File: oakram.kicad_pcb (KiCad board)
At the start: 2 copper layers, 43.2 x 54 mm, 11 parts, among them U1 IS41C16105C, U2 IS41C16105C, X1 ZIP40, X2 ZIP40

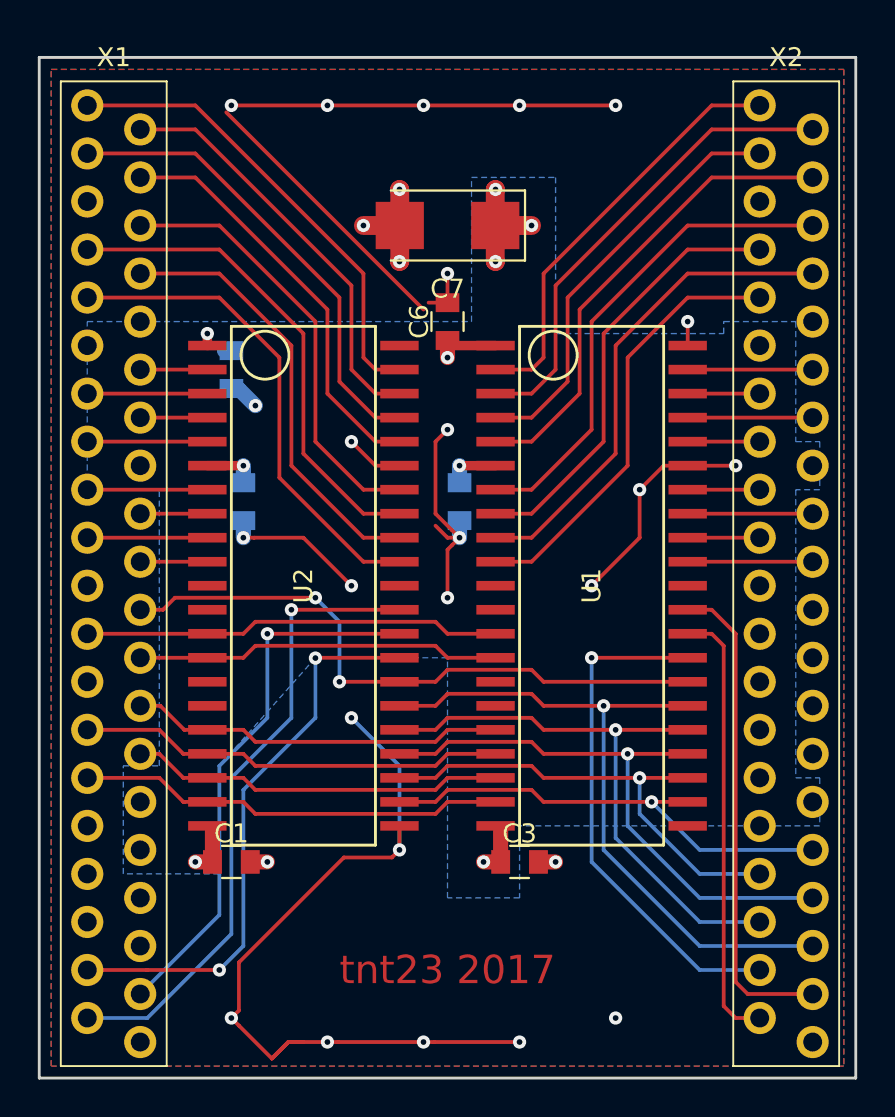
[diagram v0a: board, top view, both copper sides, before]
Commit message: Connector and chip moved
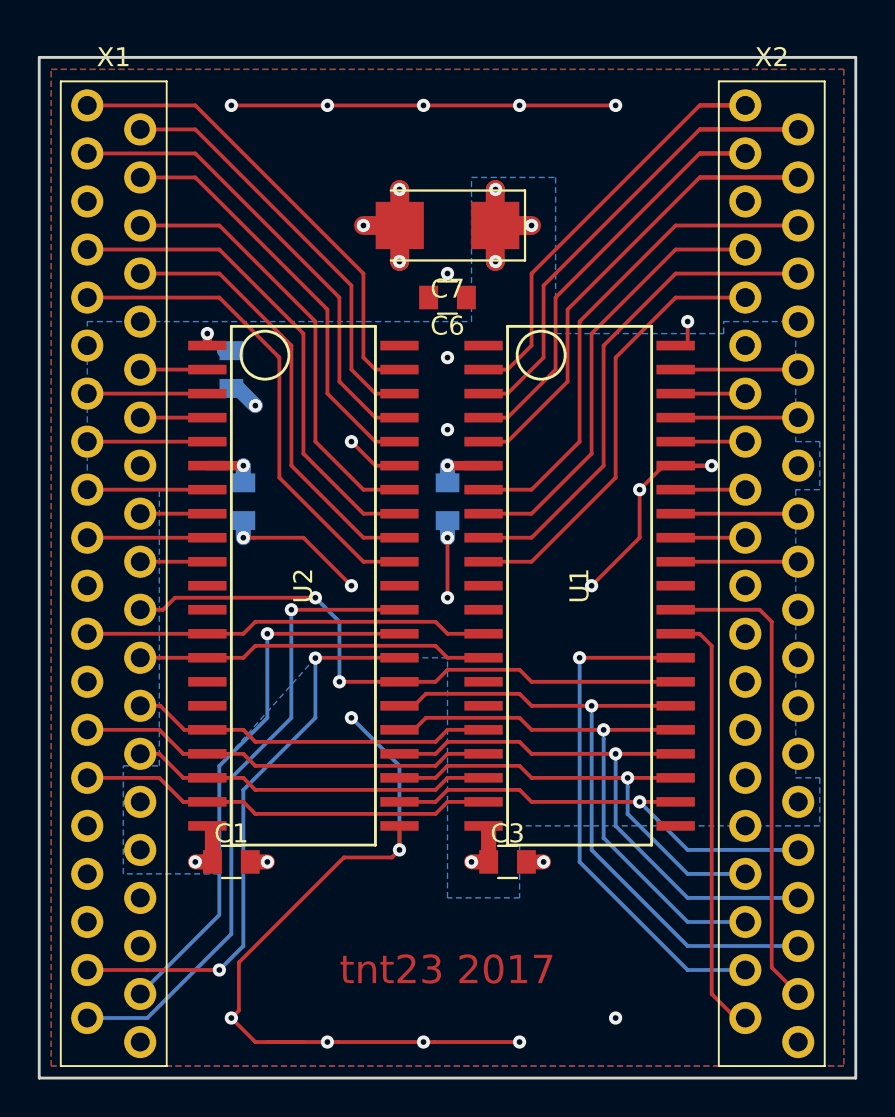
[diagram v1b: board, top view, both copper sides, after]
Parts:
- moved C6 1.27 mm to (141.0, 86.4), turned to 180 degrees
- moved X2 0.76 mm to (158.1, 100.3)
- moved C3 0.63 mm to (144.1, 116.2)
- moved C4 0.63 mm to (141.0, 97.2)
- moved U1 0.63 mm to (148.0, 101.6)
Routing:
- net VSS: track 125.6 -> 98.1 mm
- net /D25: track 24.9 -> 29.7 mm
- net VCC: track 21.8 -> 18.2 mm
- net /D27: track 25.5 -> 29.1 mm
- net /D26: track 22.4 -> 24.4 mm
- net /D24: track 22.4 -> 24.4 mm
- net /~CAS3: track 25.8 -> 25.0 mm
- net /D30: track 26.3 -> 25.5 mm
- net /A5: track 25.3 -> 26.0 mm
- net /A4: track 25.7 -> 25.1 mm
- net /~OE: track 57.2 -> 57.7 mm
- net /D21: track 6.99 -> 6.48 mm
- net /D16: track 6.99 -> 6.48 mm
- net /A8: track 36.9 -> 36.4 mm

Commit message: Board resized
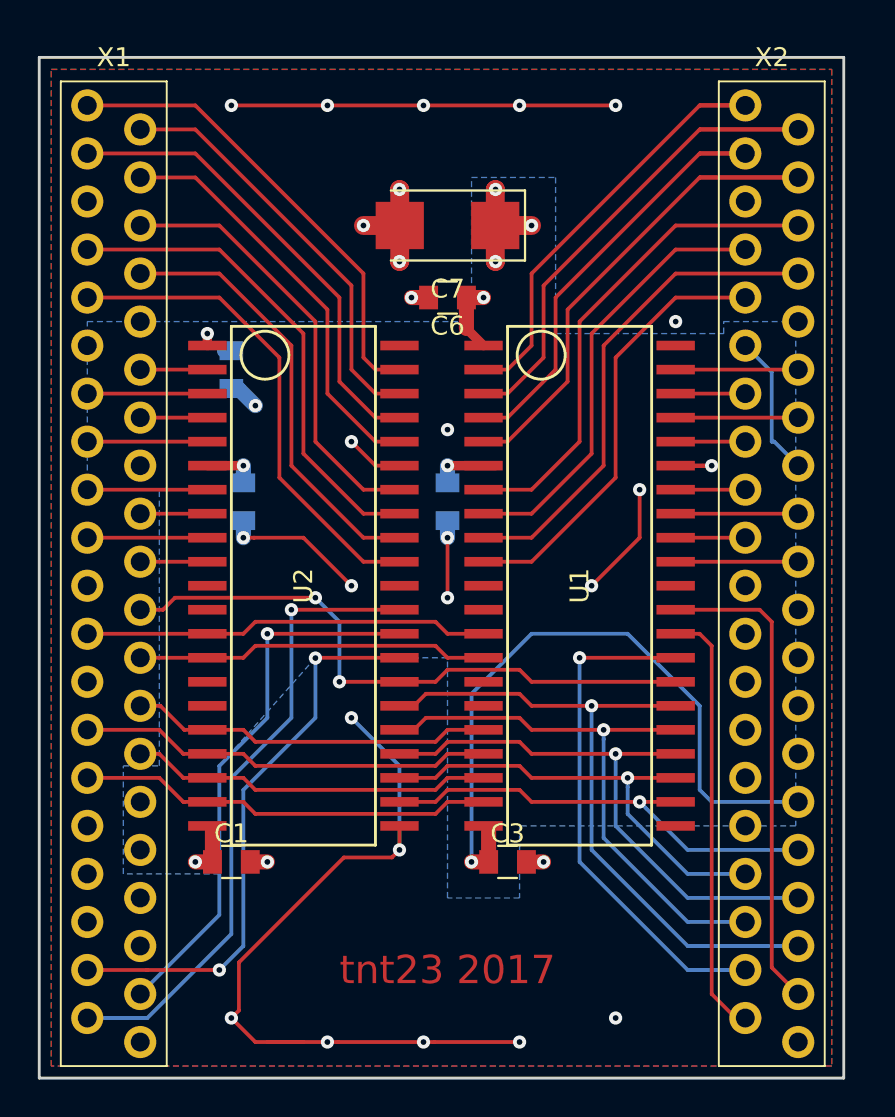
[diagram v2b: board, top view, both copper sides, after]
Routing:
- net VCC: track 18.2 -> 63.7 mm
- net VSS: track 98.1 -> 95.9 mm
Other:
- board size 43.2 x 54 mm -> 42.5 x 54 mm
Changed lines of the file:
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@@
   (thickness 1.6)
   (drawings 8)
-  (tracks 347)
+  (tracks 361)
   (zones 0)
   (modules 11)
@@
   (36 B.SilkS user)
   (37 F.SilkS user)
-  (38 B.Mask user)
-  (39 F.Mask user)
+  (38 B.Mask user hide)
+  (39 F.Mask user hide)
   (40 Dwgs.User user)
   (41 Cmts.User user)
@@
 )
 (setup
-  (last_trace_width 0.2)
+  (last_trace_width 0.8)
   (user_trace_width 0.2)
   (user_trace_width 0.3)
@@
     (effects (font (size 1.5 1.5) (thickness 0.3)))
   )
-  (dimension 43.18 (width 0.3) (layer Cmts.User)
-    (gr_text "43.180 mm" (at 140.97 134.699999) (layer Cmts.User)
+  (dimension 42.545 (width 0.3) (layer Cmts.User)
+    (gr_text "42.545 mm" (at 140.6525 134.7) (layer Cmts.User)
       (effects (font (size 1.5 1.5) (thickness 0.3)))
     )
-    (feature1 (pts (xy 162.56 127.635) (xy 162.56 136.049999)))
-    (feature2 (pts (xy 119.38 127.635) (xy 119.38 136.049999)))
-    (crossbar (pts (xy 119.38 133.349999) (xy 162.56 133.349999)))
-    (arrow1a (pts (xy 162.56 133.349999) (xy 161.433496 133.93642)))
-    (arrow1b (pts (xy 162.56 133.349999) (xy 161.433496 132.763578)))
-    (arrow2a (pts (xy 119.38 133.349999) (xy 120.506504 133.93642)))
-    (arrow2b (pts (xy 119.38 133.349999) (xy 120.506504 132.763578)))
+    (feature1 (pts (xy 161.925 127.635) (xy 161.925 136.05)))
+    (feature2 (pts (xy 119.38 127.635) (xy 119.38 136.05)))
+    (crossbar (pts (xy 119.38 133.35) (xy 161.925 133.35)))
+    (arrow1a (pts (xy 161.925 133.35) (xy 160.798496 133.936421)))
+    (arrow1b (pts (xy 161.925 133.35) (xy 160.798496 132.763579)))
+    (arrow2a (pts (xy 119.38 133.35) (xy 120.506504 133.936421)))
+    (arrow2b (pts (xy 119.38 133.35) (xy 120.506504 132.763579)))
   )
   (dimension 53.975 (width 0.3) (layer Cmts.User)
-    (gr_text "53.975 mm" (at 172.8 100.6475 270) (layer Cmts.User)
+    (gr_text "53.975 mm" (at 172.165 100.6475 270) (layer Cmts.User)
       (effects (font (size 1.5 1.5) (thickness 0.3)))
     )
-    (feature1 (pts (xy 162.56 127.635) (xy 174.15 127.635)))
-    (feature2 (pts (xy 162.56 73.66) (xy 174.15 73.66)))
-    (crossbar (pts (xy 171.45 73.66) (xy 171.45 127.635)))
-    (arrow1a (pts (xy 171.45 127.635) (xy 170.863579 126.508496)))
-    (arrow1b (pts (xy 171.45 127.635) (xy 172.036421 126.508496)))
-    (arrow2a (pts (xy 171.45 73.66) (xy 170.863579 74.786504)))
-    (arrow2b (pts (xy 171.45 73.66) (xy 172.036421 74.786504)))
+    (feature1 (pts (xy 161.925 127.635) (xy 173.515 127.635)))
+    (feature2 (pts (xy 161.925 73.66) (xy 173.515 73.66)))
+    (crossbar (pts (xy 170.815 73.66) (xy 170.815 127.635)))
+    (arrow1a (pts (xy 170.815 127.635) (xy 170.228579 126.508496)))
+    (arrow1b (pts (xy 170.815 127.635) (xy 171.401421 126.508496)))
+    (arrow2a (pts (xy 170.815 73.66) (xy 170.228579 74.786504)))
+    (arrow2b (pts (xy 170.815 73.66) (xy 171.401421 74.786504)))
   )
   (gr_line (start 119.38 127.635) (end 119.38 73.66) (layer Edge.Cuts) (width 0.15))
-  (gr_line (start 162.56 127.635) (end 119.38 127.635) (layer Edge.Cuts) (width 0.15))
-  (gr_line (start 162.56 73.66) (end 162.56 127.635) (layer Edge.Cuts) (width 0.15))
-  (gr_line (start 119.38 73.66) (end 162.56 73.66) (layer Edge.Cuts) (width 0.15))
+  (gr_line (start 161.925 127.635) (end 119.38 127.635) (layer Edge.Cuts) (width 0.15))
+  (gr_line (start 161.925 73.66) (end 161.925 127.635) (layer Edge.Cuts) (width 0.15))
+  (gr_line (start 119.38 73.66) (end 161.925 73.66) (layer Edge.Cuts) (width 0.15))
   (segment (start 138.43 90.17) (end 137.16 90.17) (width 0.2) (layer F.Cu) (net 1))
   (segment (start 137.16 90.17) (end 136.525 89.535) (width 0.2) (layer F.Cu) (net 1))
@@
   (segment (start 145.415 85.09) (end 154.305 76.2) (width 0.2) (layer F.Cu) (net 55))
   (segment (start 154.305 76.2) (end 157.48 76.2) (width 0.2) (layer F.Cu) (net 55))
+  (segment (start 139.97 86.36) (end 139.065 86.36) (width 0.8) (layer F.Cu) (net 56))
+  (via (at 153.035 87.63) (size 0.7) (drill 0.3) (layers F.Cu B.Cu) (net 56))
   (segment (start 154.445026 95.25) (end 154.94 95.25) (width 0.2) (layer F.Cu) (net 56))
   (segment (start 152.4 95.25) (end 154.445026 95.25) (width 0.2) (layer F.Cu) (net 56))
-  (segment (start 151.13 96.52) (end 152.4 95.25) (width 0.2) (layer F.Cu) (net 56))
   (segment (start 153.67 95.25) (end 154.94 95.25) (width 0.2) (layer F.Cu) (net 56))
   (via (at 154.94 95.25) (size 0.7) (drill 0.3) (layers F.Cu B.Cu) (net 56))
@@
   (segment (start 129.939999 124.059999) (end 129.54 124.459998) (width 0.2) (layer F.Cu) (net 56))
   (via (at 140.97 93.345) (size 0.7) (drill 0.3) (layers F.Cu B.Cu) (net 56))
-  (via (at 153.67 87.63) (size 0.7) (drill 0.3) (layers F.Cu B.Cu) (net 56))
-  (segment (start 153.67 88.9) (end 153.67 87.63) (width 0.2) (layer F.Cu) (net 56))
   (via (at 149.86 124.46) (size 0.7) (drill 0.3) (layers F.Cu B.Cu) (net 56))
   (segment (start 130.740685 99.06) (end 130.175 99.06) (width 0.2) (layer F.Cu) (net 56))
@@
   (via (at 129.54 76.2) (size 0.7) (drill 0.3) (layers F.Cu B.Cu) (net 56))
   (via (at 140.97 102.235) (size 0.7) (drill 0.3) (layers F.Cu B.Cu) (net 56))
-  (via (at 140.97 85.09) (size 0.7) (drill 0.3) (layers F.Cu B.Cu) (net 56))
+  (via (at 139.065 86.36) (size 0.7) (drill 0.3) (layers F.Cu B.Cu) (net 56))
   (segment (start 138.43 114.3) (end 138.43 115.57) (width 0.2) (layer F.Cu) (net 56))
   (via (at 138.43 115.57) (size 0.7) (drill 0.3) (layers F.Cu B.Cu) (net 56))
@@
   (segment (start 130.54 116.205) (end 131.445 116.205) (width 0.8) (layer F.Cu) (net 56))
   (via (at 131.445 116.205) (size 0.7) (drill 0.3) (layers F.Cu B.Cu) (net 56))
+  (segment (start 142.875 86.36) (end 141.97 86.36) (width 0.8) (layer F.Cu) (net 57))
+  (via (at 142.875 86.36) (size 0.7) (drill 0.3) (layers F.Cu B.Cu) (net 57))
+  (segment (start 141.97 86.36) (end 141.97 87.995) (width 0.8) (layer F.Cu) (net 57))
+  (segment (start 141.97 87.995) (end 142.875 88.9) (width 0.5) (layer F.Cu) (net 57))
+  (segment (start 142.24 116.205) (end 142.24 107.315) (width 0.2) (layer B.Cu) (net 57))
+  (segment (start 145.415 104.14) (end 150.495 104.14) (width 0.2) (layer B.Cu) (net 57))
+  (segment (start 154.305 112.395) (end 154.94 113.03) (width 0.2) (layer B.Cu) (net 57))
+  (segment (start 142.24 107.315) (end 145.415 104.14) (width 0.2) (layer B.Cu) (net 57))
+  (segment (start 150.495 104.14) (end 154.305 107.95) (width 0.2) (layer B.Cu) (net 57))
+  (segment (start 154.305 107.95) (end 154.305 112.395) (width 0.2) (layer B.Cu) (net 57))
+  (segment (start 154.94 113.03) (end 159.518 113.03) (width 0.2) (layer B.Cu) (net 57))
+  (segment (start 143.145 114.57) (end 142.875 114.3) (width 0.2) (layer F.Cu) (net 57))
+  (segment (start 158.115 93.98) (end 158.248 93.98) (width 0.2) (layer B.Cu) (net 57))
+  (segment (start 158.248 93.98) (end 159.518 95.25) (width 0.2) (layer B.Cu) (net 57))
+  (segment (start 158.115 90.297) (end 158.115 93.98) (width 0.2) (layer B.Cu) (net 57))
+  (segment (start 156.718 88.9) (end 158.115 90.297) (width 0.2) (layer B.Cu) (net 57))
   (segment (start 142.875 116.205) (end 142.24 116.205) (width 0.8) (layer F.Cu) (net 57))
   (via (at 142.24 116.205) (size 0.7) (drill 0.3) (layers F.Cu B.Cu) (net 57))
@@
   (segment (start 143.495 82.55) (end 145.415 82.55) (width 1) (layer F.Cu) (net 57))
   (via (at 145.415 82.55) (size 0.7) (drill 0.3) (layers F.Cu B.Cu) (net 57))
-  (via (at 140.97 89.535) (size 0.7) (drill 0.3) (layers F.Cu B.Cu) (net 57))
   (segment (start 129.54 89.17) (end 129.175 89.17) (width 0.8) (layer B.Cu) (net 57))
   (segment (start 128.54 116.205) (end 127.635 116.205) (width 0.8) (layer F.Cu) (net 57))
@@
     (connect_pads (clearance 0.254))
     (min_thickness 0.254)
-    (fill (arc_segments 32) (thermal_gap 0.254) (thermal_bridge_width 0.508))
+    (fill yes (arc_segments 32) (thermal_gap 0.254) (thermal_bridge_width 0.508))
     (polygon
       (pts
-        (xy 120.015 74.295) (xy 161.925 74.295) (xy 161.925 127) (xy 120.015 127)
+        (xy 120.015 74.295) (xy 161.29 74.295) (xy 161.29 127) (xy 120.015 127)
       )
     )
@@
     (connect_pads (clearance 0.254))
     (min_thickness 0.254)
-    (fill (arc_segments 32) (thermal_gap 0.254) (thermal_bridge_width 0.508))
+    (fill yes (arc_segments 32) (thermal_gap 0.254) (thermal_bridge_width 0.508))
     (polygon
       (pts
         (xy 123.825 111.125) (xy 125.73 111.125) (xy 125.73 96.52) (xy 121.92 96.52) (xy 121.92 87.63)
         (xy 142.24 87.63) (xy 142.24 80.01) (xy 146.685 80.01) (xy 146.685 88.265) (xy 155.575 88.265)
-        (xy 155.575 87.63) (xy 159.385 87.63) (xy 159.385 93.98) (xy 160.655 93.98) (xy 160.655 96.52)
-        (xy 159.385 96.52) (xy 159.385 111.76) (xy 160.655 111.76) (xy 160.655 114.3) (xy 144.78 114.3)
-        (xy 144.78 118.11) (xy 140.97 118.11) (xy 140.97 105.41) (xy 133.985 105.41) (xy 128.905 111.125)
-        (xy 128.905 116.84) (xy 123.825 116.84)
+        (xy 155.575 87.63) (xy 159.385 87.63) (xy 159.385 114.3) (xy 144.78 114.3) (xy 144.78 118.11)
+        (xy 140.97 118.11) (xy 140.97 105.41) (xy 133.985 105.41) (xy 128.905 111.125) (xy 128.905 116.84)
+        (xy 123.825 116.84)
       )
     )
@@
     (connect_pads (clearance 0.254))
     (min_thickness 0.254)
-    (fill (arc_segments 32) (thermal_gap 0.254) (thermal_bridge_width 0.508))
+    (fill yes (arc_segments 32) (thermal_gap 0.254) (thermal_bridge_width 0.508))
     (polygon
       (pts
-        (xy 120.015 74.295) (xy 161.925 74.295) (xy 161.925 127) (xy 120.015 127)
+        (xy 120.015 74.295) (xy 161.29 74.295) (xy 161.29 127) (xy 120.015 127)
       )
     )
@@
     (connect_pads (clearance 0.254))
     (min_thickness 0.254)
-    (fill (arc_segments 16) (thermal_gap 0.508) (thermal_bridge_width 0.508))
+    (fill yes (arc_segments 16) (thermal_gap 0.508) (thermal_bridge_width 0.508))
     (polygon
       (pts
